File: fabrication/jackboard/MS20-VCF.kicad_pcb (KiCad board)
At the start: 2 copper layers, 50 x 110 mm, 55 parts, among them J5 Power Input, J6 FilterCV1, J7 FilterIn1, J8 FilterOut1, Q1 BC559, Q2 BC559, SW1 Hpass/Lpass Switch, U1 LM13700, U2 TL072

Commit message: update readme and kicab pcb for jackboard (fix 3d parts issue)
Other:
- board text removed: "12HP"
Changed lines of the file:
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@@
       (drillshape 0)
       (scaleselection 1)
-      (outputdirectory "Gerber/")
+      (outputdirectory "")
     )
   )
@@
     (pad "3" thru_hole circle (at 0 -5 90) (size 1.8 1.8) (drill 1) (layers *.Cu *.Mask)
       (net 1 "GND") (pinfunction "3") (pintype "passive"))
-    (model "${KICAD6_3DMODEL_DIR}/Potentiometer_THT.3dshapes/RK09K1130AH1.STEP"
+    (model "${KIPRJMOD}/3D/RK09K1130AH1.STEP"
       (offset (xyz 7 2.5 0))
       (scale (xyz 1 1 1))
@@
     (pad "3" thru_hole circle (at 0 -5 90) (size 1.8 1.8) (drill 1) (layers *.Cu *.Mask)
       (net 18 "Net-(R18-Pad2)") (pinfunction "3") (pintype "passive"))
-    (model "${KICAD6_3DMODEL_DIR}/Potentiometer_THT.3dshapes/RK09K1130AH1.STEP"
+    (model "${KIPRJMOD}/3D/RK09K1130AH1.STEP"
       (offset (xyz 7 2.5 0))
       (scale (xyz 1 1 1))
@@
     (pad "TN" thru_hole circle (at 0 3.1 180) (size 2.13 2.13) (drill 1.42) (layers *.Cu *.Mask)
       (net 40 "unconnected-(J6-PadTN)") (pintype "passive+no_connect"))
-    (model "${KICAD6_3DMODEL_DIR}/Connector_BarrelJack.3dshapes/PJ301M-12 Thonkiconn v0.2.stp"
+    (model "${KIPRJMOD}/3D/PJ301M-12 Thonkiconn v0.2.stp"
       (offset (xyz 0 -7 0))
       (scale (xyz 1 1 1))
@@
     (pad "TN" thru_hole circle (at 0 3.1 180) (size 2.13 2.13) (drill 1.42) (layers *.Cu *.Mask)
       (net 41 "unconnected-(J7-PadTN)") (pintype "passive+no_connect"))
-    (model "${KICAD6_3DMODEL_DIR}/Connector_BarrelJack.3dshapes/PJ301M-12 Thonkiconn v0.2.stp"
+    (model "${KIPRJMOD}/3D/PJ301M-12 Thonkiconn v0.2.stp"
       (offset (xyz 0 -7 0))
       (scale (xyz 1 1 1))
@@
     (pad "TN" thru_hole circle (at 0 3.1 180) (size 2.13 2.13) (drill 1.42) (layers *.Cu *.Mask)
       (net 42 "unconnected-(J8-PadTN)") (pintype "passive+no_connect"))
-    (model "${KICAD6_3DMODEL_DIR}/Connector_BarrelJack.3dshapes/PJ301M-12 Thonkiconn v0.2.stp"
+    (model "${KIPRJMOD}/3D/PJ301M-12 Thonkiconn v0.2.stp"
       (offset (xyz 0 -7 0))
       (scale (xyz 1 1 1))
@@
     (pad "3" thru_hole circle (at 0 -5 90) (size 1.8 1.8) (drill 1) (layers *.Cu *.Mask)
       (net 1 "GND") (pinfunction "3") (pintype "passive"))
-    (model "${KICAD6_3DMODEL_DIR}/Potentiometer_THT.3dshapes/RK09K1130AH1.STEP"
+    (model "${KIPRJMOD}/3D/RK09K1130AH1.STEP"
       (offset (xyz 7 2.5 0))
       (scale (xyz 1 1 1))
@@
     (pad "6" thru_hole oval (at -4.7 2.4 180) (size 3.7 2.4) (drill oval 2.2 1) (layers *.Cu *.Mask)
       (net 1 "GND") (pinfunction "C") (pintype "passive"))
-    (model "${KICAD6_3DMODEL_DIR}/Button_Switch_THT.3dshapes/Toggle Switch - Double .step"
+    (model "${KIPRJMOD}/3D/Toggle Switch - Double .step"
       (offset (xyz 0 0 0))
       (scale (xyz 1 1 1))
@@
     (fp_line (start -1.45 2.75) (end -1.45 -2.75) (layer "B.CrtYd") (width 0.05))
     (fp_line (start -0.73 1.32665) (end -0.73 -1.32665) (layer "B.Fab") (width 0.1))
-    (fp_arc (start -0.730339 -1.32614) (mid 3.670001 -0.000306) (end -0.73 1.32665) (layer "B.Fab") (width 0.1))
+    (fp_arc (start -0.730339 -1.32614) (mid 3.67 -0.000308) (end -0.73 1.32665) (layer "B.Fab") (width 0.1))
     (fp_circle (center 1.27 0) (end 3.27 0) (layer "B.Fab") (width 0.1) (fill none))
     (pad "1" thru_hole rect (at 0 0 90) (size 1.8 1.8) (drill 0.9) (layers *.Cu *.Mask)
@@
     (fp_line (start 4.52 3.91) (end 4.52 -14.07) (layer "B.Fab") (width 0.1))
     (fp_line (start -1.98 -14.07) (end -1.98 -7.13) (layer "B.Fab") (width 0.1))
-    (pad "1" thru_hole roundrect (at 0 0 270) (size 1.7 1.7) (drill 1) (layers *.Cu *.Mask) (roundrect_rratio 0.1470588235)
+    (pad "1" thru_hole roundrect (at 0 0 270) (size 1.7 1.7) (drill 1) (layers *.Cu *.Mask) (roundrect_rratio 0.147059)
       (net 26 "Net-(FB2-Pad2)") (pinfunction "Pin_1") (pintype "passive"))
     (pad "2" thru_hole circle (at 2.54 0 270) (size 1.7 1.7) (drill 1) (layers *.Cu *.Mask)
@@
     )
   )
-  (gr_line (start 30 25) (end 30 31) (layer "Dwgs.User") (width 0.05))
   (gr_line (start 42 110) (end 42 143) (layer "Dwgs.User") (width 0.1))
   (gr_line (start 85 36.5) (end 85 146.5) (layer "Edge.Cuts") (width 0.05))
@@
     (effects (font (size 1 1) (thickness 0.15)))
   )
-  (gr_text "12HP\n" (at 62 32.5) (layer "Dwgs.User")
-    (effects (font (size 1 1) (thickness 0.15)))
-  )
-  (dimension (type aligned) (layer "Dwgs.User")
-    (pts (xy 30 25) (xy 30 158))
-    (height 8)
-    (gr_text "133.0000 mm" (at 20.85 91.5 90) (layer "Dwgs.User")
-      (effects (font (size 1 1) (thickness 0.15)))
-    )
-    (format (units 2) (units_format 1) (precision 4))
-    (style (thickness 0.15) (arrow_length 1.27) (text_position_mode 0) (extension_height 0.58642) (extension_offset 0) keep_text_aligned)
-  )
-  (dimension (type aligned) (layer "Dwgs.User")
-    (pts (xy 33 31) (xy 33 25))
-    (height -6)
-    (gr_text "6.0000 mm" (at 25.85 28 90) (layer "Dwgs.User")
-      (effects (font (size 1 1) (thickness 0.15)))
-    )
-    (format (units 2) (units_format 1) (precision 4))
-    (style (thickness 0.15) (arrow_length 1.27) (text_position_mode 0) (extension_height 0.58642) (extension_offset 0) keep_text_aligned)
-  )
   (segment (start 56.219954 78.2) (end 56.195388 78.224566) (width 0.3) (layer "F.Cu") (net 2))

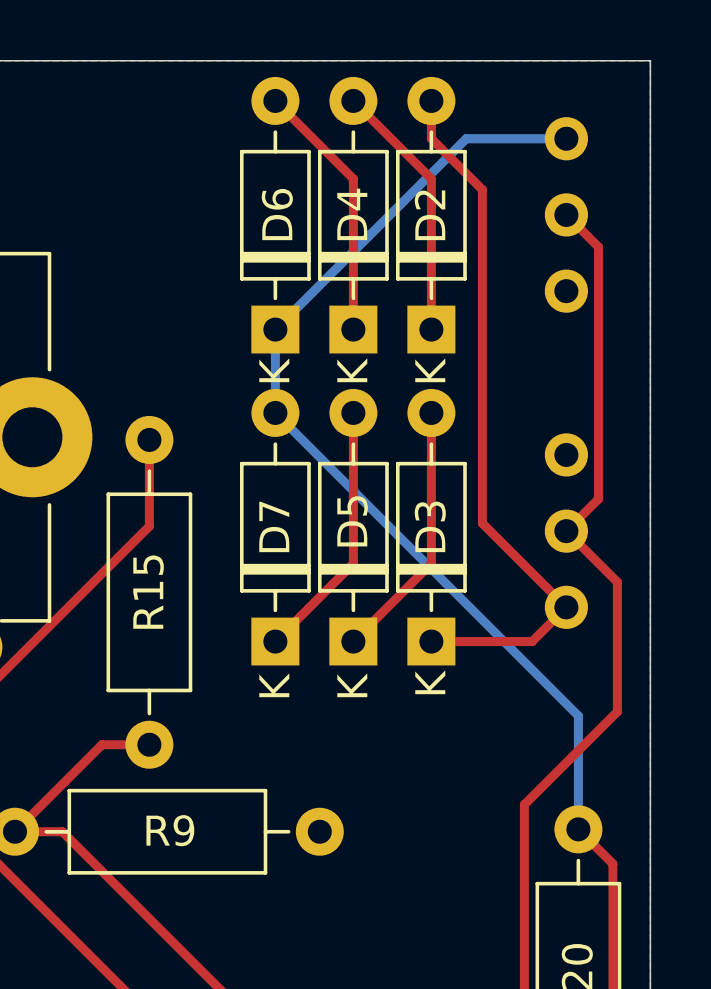
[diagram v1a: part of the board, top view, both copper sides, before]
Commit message: update footprint trimmer
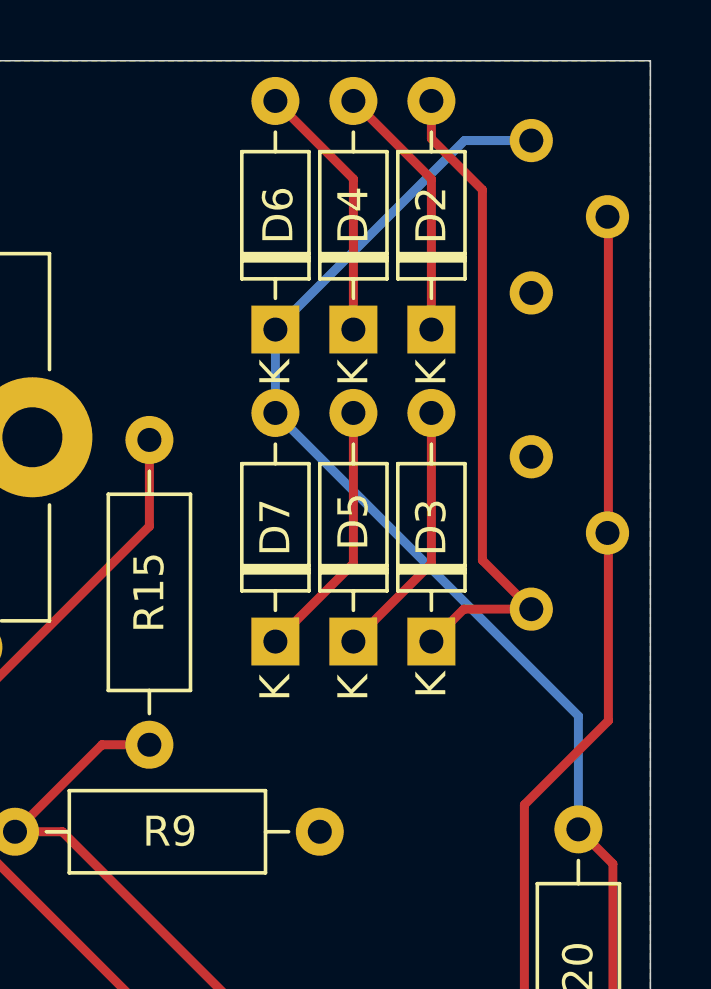
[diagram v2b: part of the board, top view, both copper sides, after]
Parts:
- C2, C3: value 10µ -> 10uF
- C6: value 10µF -> 10uF
- ResLv1: value 3.3k -> 10k; footprint Potentiometer_THT:Potentiometer_Bourns_3386C_Horizontal -> Potentiometer_THT:Potentiometer_Bourns_3386X_Horizontal
- ResVol1: footprint Potentiometer_THT:Potentiometer_Bourns_3386C_Horizontal -> Potentiometer_THT:Potentiometer_Bourns_3386X_Horizontal
- moved ResLv1 1.17 mm to (81.0, 44.2)
- moved ResVol1 1.17 mm to (81.0, 54.8)
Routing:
- net Net-(C1-Pad2): track 86.2 -> 84.5 mm
- net Net-(D2-Pad2): track 23.7 -> 22.1 mm
- net Net-(D6-Pad1): track 69.0 -> 67.8 mm
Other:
- board text added: "12HP"

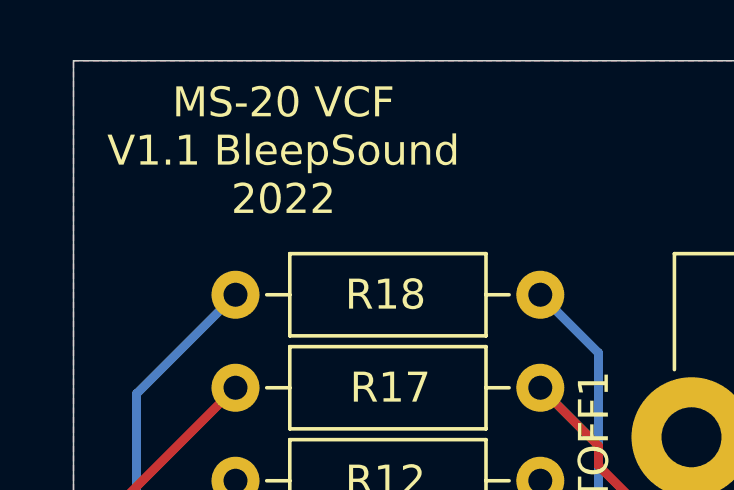
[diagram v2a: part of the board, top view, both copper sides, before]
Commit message: update to v1.2 on silkscreen
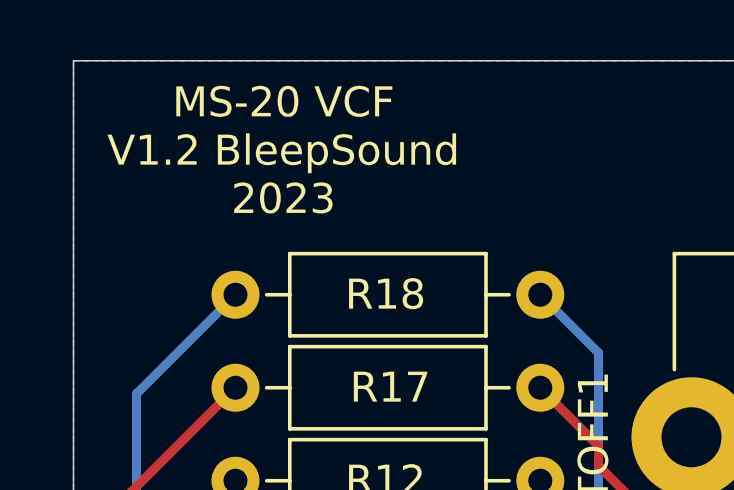
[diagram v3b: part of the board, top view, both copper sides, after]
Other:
- board text added: "MS-20 VCF V1.2 BleepSound 2023"
- board text removed: "MS-20 VCF V1.1 BleepSound 2022"
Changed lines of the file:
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@@
     )
   )
+  (gr_circle (center 42 81.06) (end 42.1 81.16) (layer "B.SilkS") (width 0.12) (fill none))
   (gr_line (start 42 110) (end 42 143) (layer "Dwgs.User") (width 0.1))
   (gr_line (start 85 36.5) (end 85 146.5) (layer "Edge.Cuts") (width 0.05))
@@
     (effects (font (size 1.5 1.5) (thickness 0.3)) (justify mirror))
   )
-  (gr_text "MS-20 VCF\nV1.1 BleepSound\n2022" (at 42 39.5) (layer "F.SilkS")
+  (gr_text "MS-20 VCF\nV1.2 BleepSound\n2023" (at 42 39.5) (layer "F.SilkS")
     (effects (font (size 1 1) (thickness 0.15)))
   )

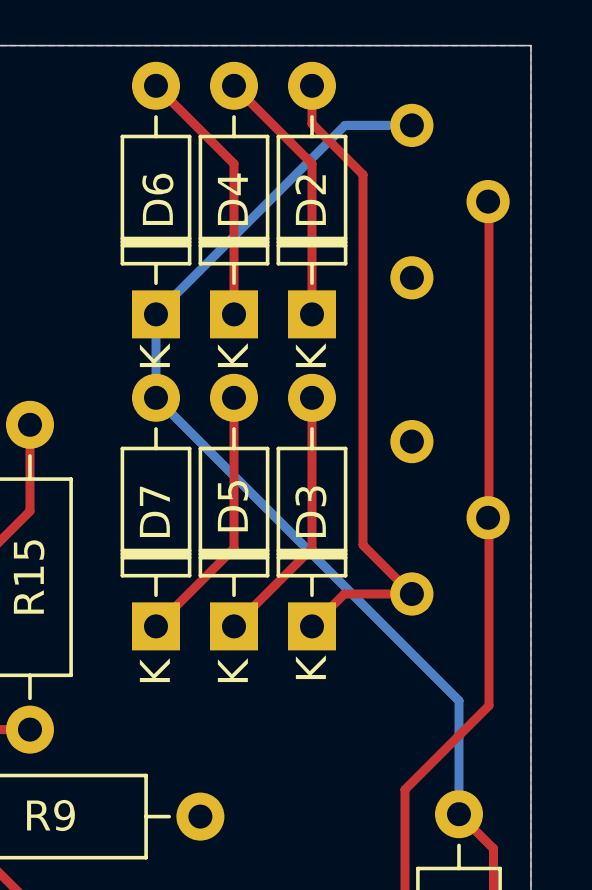
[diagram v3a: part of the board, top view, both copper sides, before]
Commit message: update footprint for trimmer
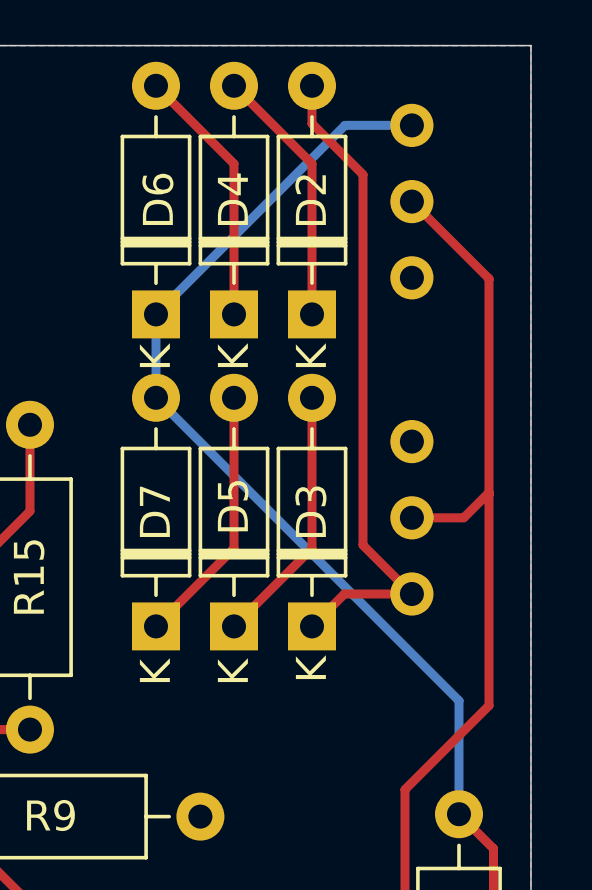
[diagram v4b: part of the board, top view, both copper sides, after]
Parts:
- ResLv1, ResVol1: footprint Potentiometer_THT:Potentiometer_Bourns_3386X_Horizontal -> Potentiometer_THT:Potentiometer_Bourns_3386C_Horizontal
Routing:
- net Net-(C1-Pad2): track 84.5 -> 88.5 mm
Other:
- board text removed: "12HP"
